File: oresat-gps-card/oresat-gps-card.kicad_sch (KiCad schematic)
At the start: 0 parts

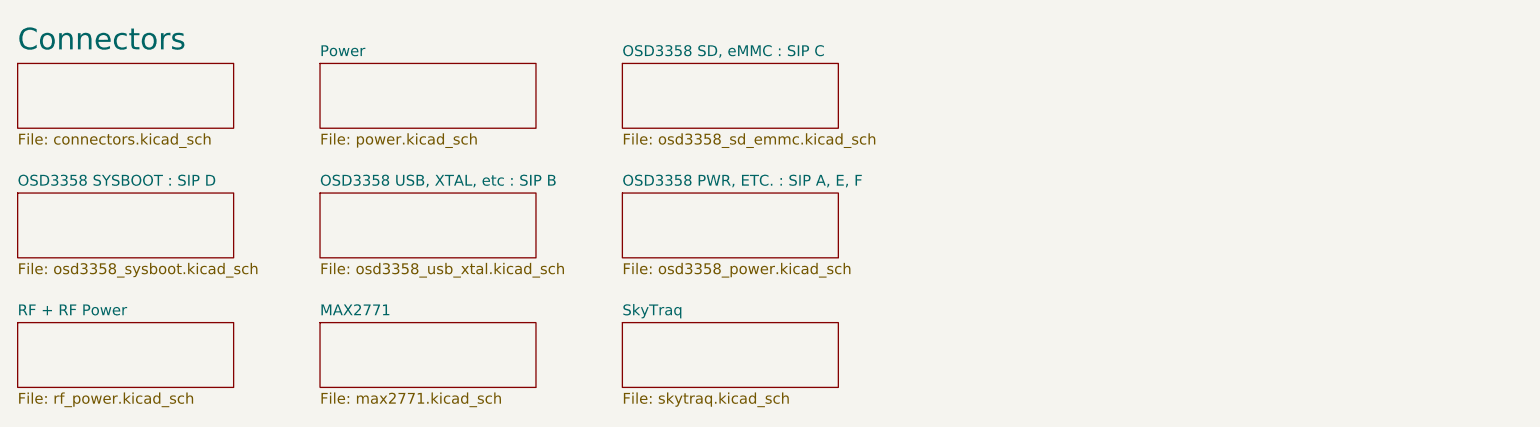
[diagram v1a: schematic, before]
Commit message: Updated schematic sheet links to match new naming
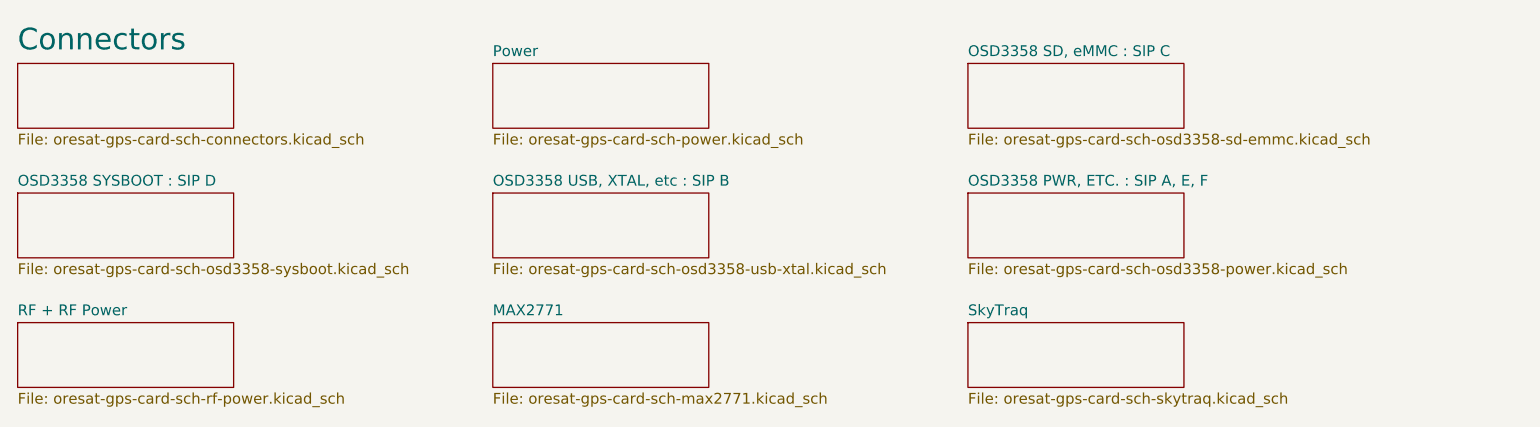
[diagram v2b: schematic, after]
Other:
- sheet Connectors: file connectors.kicad_sch -> oresat-gps-card-sch-connectors.kicad_sch
- sheet MAX2771: file max2771.kicad_sch -> oresat-gps-card-sch-max2771.kicad_sch
- sheet OSD3358 PWR, ETC. : SIP A, E, F: file osd3358_power.kicad_sch -> oresat-gps-card-sch-osd3358-power.kicad_sch
- sheet OSD3358 SD, eMMC : SIP C: file osd3358_sd_emmc.kicad_sch -> oresat-gps-card-sch-osd3358-sd-emmc.kicad_sch
- sheet OSD3358 SYSBOOT : SIP D: file osd3358_sysboot.kicad_sch -> oresat-gps-card-sch-osd3358-sysboot.kicad_sch
- sheet OSD3358 USB, XTAL, etc : SIP B: file osd3358_usb_xtal.kicad_sch -> oresat-gps-card-sch-osd3358-usb-xtal.kicad_sch
- sheet Power: file power.kicad_sch -> oresat-gps-card-sch-power.kicad_sch
- sheet RF + RF Power: file rf_power.kicad_sch -> oresat-gps-card-sch-rf-power.kicad_sch
- sheet SkyTraq: file skytraq.kicad_sch -> oresat-gps-card-sch-skytraq.kicad_sch

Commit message: Updated KiCAD 8, updated schematic sheet info, polished some schematic things, and made DNP parts DNP.
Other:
- title: (none) -> OreSat GPS Card

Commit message: Routine push
Began update to GPS chip
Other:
- removed sheet MAX2771
- added sheet MAX2769 (oresat-gps-card-sch-max2771.kicad_sch)
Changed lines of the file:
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@@
 (kicad_sch
-	(version 20250114)
+	(version 20260306)
 	(generator "eeschema")
-	(generator_version "9.0")
+	(generator_version "10.0")
 	(paper "B")
 	(title_block
@@
 		)
 		(fill
-			(color 0 0 0 0.0000)
+			(color 0 0 0 0)
 		)
 		(property "Sheetname" "OSD3358 PWR, ETC. : SIP A, E, F"
 			(at 185.42 80.5684 0)
+			(show_name no)
+			(do_not_autoplace no)
 			(effects
 				(font
@@
 		(property "Sheetfile" "oresat-gps-card-sch-osd3358-power.kicad_sch"
 			(at 185.42 89.4846 0)
+			(show_name no)
+			(do_not_autoplace no)
 			(effects
 				(font
@@
 		)
 		(fill
-			(color 0 0 0 0.0000)
+			(color 0 0 0 0)
 		)
 		(property "Sheetname" "OSD3358 SYSBOOT : SIP D"
 			(at 73.66 80.5684 0)
+			(show_name no)
+			(do_not_autoplace no)
 			(effects
 				(font
@@
 		(property "Sheetfile" "oresat-gps-card-sch-osd3358-sysboot.kicad_sch"
 			(at 73.66 89.4846 0)
+			(show_name no)
+			(do_not_autoplace no)
 			(effects
 				(font
@@
 		)
 		(fill
-			(color 0 0 0 0.0000)
+			(color 0 0 0 0)
 		)
 		(property "Sheetname" "OSD3358 USB, XTAL, etc : SIP B"
 			(at 129.54 80.5684 0)
+			(show_name no)
+			(do_not_autoplace no)
 			(effects
 				(font
@@
 		(property "Sheetfile" "oresat-gps-card-sch-osd3358-usb-xtal.kicad_sch"
 			(at 129.54 89.4846 0)
+			(show_name no)
+			(do_not_autoplace no)
 			(effects
 				(font
@@
 	)
 	(sheet
+		(at 129.54 66.04)
+		(size 25.4 7.62)
+		(exclude_from_sim no)
+		(in_bom yes)
+		(on_board yes)
+		(dnp no)
+		(fields_autoplaced yes)
+		(stroke
+			(width 0.1524)
+			(type solid)
+		)
+		(fill
+			(color 0 0 0 0)
+		)
+		(property "Sheetname" "Power"
+			(at 129.54 65.3284 0)
+			(show_name no)
+			(do_not_autoplace no)
+			(effects
+				(font
+					(size 1.27 1.27)
+				)
+				(justify left bottom)
+			)
+		)
+		(property "Sheetfile" "oresat-gps-card-sch-power.kicad_sch"
+			(at 129.54 74.2446 0)
+			(show_name no)
+			(do_not_autoplace no)
+			(effects
+				(font
+					(size 1.27 1.27)
+				)
+				(justify left top)
+			)
+		)
+		(instances
+			(project "oresat-gps-card"
+				(path "/65d12cdd-c326-4033-9053-c59fa4e0b25e"
+					(page "2")
+				)
+			)
+		)
+	)
+	(sheet
 		(at 129.54 96.52)
 		(size 25.4 7.62)
@@
 		)
 		(fill
-			(color 0 0 0 0.0000)
-		)
-		(property "Sheetname" "MAX2771"
+			(color 0 0 0 0)
+		)
+		(property "Sheetname" "MAX2769"
 			(at 129.54 95.8084 0)
+			(show_name no)
+			(do_not_autoplace no)
 			(effects
 				(font
@@
 		(property "Sheetfile" "oresat-gps-card-sch-max2771.kicad_sch"
 			(at 129.54 104.7246 0)
-			(effects
-				(font
-					(size 1.27 1.27)
-				)
-				(justify left top)
-			)
-		)
-		(instances
-			(project "oresat-gps-card"
-				(path "/65d12cdd-c326-4033-9053-c59fa4e0b25e"
-					(page "8")
-				)
-			)
-		)
-	)
-	(sheet
-		(at 129.54 66.04)
-		(size 25.4 7.62)
-		(exclude_from_sim no)
-		(in_bom yes)
-		(on_board yes)
-		(dnp no)
-		(fields_autoplaced yes)
-		(stroke
-			(width 0.1524)
-			(type solid)
-		)
-		(fill
-			(color 0 0 0 0.0000)
-		)
-		(property "Sheetname" "Power"
-			(at 129.54 65.3284 0)
-			(effects
-				(font
-					(size 1.27 1.27)
-				)
-				(justify left bottom)
-			)
-		)
-		(property "Sheetfile" "oresat-gps-card-sch-power.kicad_sch"
-			(at 129.54 74.2446 0)
-			(effects
-				(font
-					(size 1.27 1.27)
-				)
-				(justify left top)
-			)
-		)
-		(instances
-			(project "oresat-gps-card"
-				(path "/65d12cdd-c326-4033-9053-c59fa4e0b25e"
-					(page "2")
+			(show_name no)
+			(do_not_autoplace no)
+			(effects
+				(font
+					(size 1.27 1.27)
+				)
+				(justify left top)
+			)
+		)
+		(instances
+			(project "oresat-gps-card"
+				(path "/65d12cdd-c326-4033-9053-c59fa4e0b25e"
+					(page "10")
 				)
 			)
@@
 		)
 		(fill
-			(color 0 0 0 0.0000)
+			(color 0 0 0 0)
 		)
 		(property "Sheetname" "RF + RF Power"
 			(at 73.66 95.8084 0)
+			(show_name no)
+			(do_not_autoplace no)
 			(effects
 				(font
@@
 		(property "Sheetfile" "oresat-gps-card-sch-rf-power.kicad_sch"
 			(at 73.66 104.7246 0)
+			(show_name no)
+			(do_not_autoplace no)
 			(effects
 				(font
@@
 		)
 		(fill
-			(color 0 0 0 0.0000)
+			(color 0 0 0 0)
 		)
 		(property "Sheetname" "Connectors"
 			(at 73.66 64.6934 0)
+			(show_name no)
+			(do_not_autoplace no)
 			(effects
 				(font
@@
 		(property "Sheetfile" "oresat-gps-card-sch-connectors.kicad_sch"
 			(at 73.66 74.2446 0)
+			(show_name no)
+			(do_not_autoplace no)
 			(effects
 				(font
@@
 		)
 		(fill
-			(color 0 0 0 0.0000)
+			(color 0 0 0 0)
 		)
 		(property "Sheetname" "OSD3358 SD, eMMC : SIP C"
 			(at 185.42 65.3284 0)
+			(show_name no)
+			(do_not_autoplace no)
 			(effects
 				(font
@@
 		(property "Sheetfile" "oresat-gps-card-sch-osd3358-sd-emmc.kicad_sch"
 			(at 185.42 74.2446 0)
+			(show_name no)
+			(do_not_autoplace no)
 			(effects
 				(font
@@
 		)
 		(fill
-			(color 0 0 0 0.0000)
+			(color 0 0 0 0)
 		)
 		(property "Sheetname" "SkyTraq"
 			(at 185.42 95.8084 0)
+			(show_name no)
+			(do_not_autoplace no)
 			(effects
 				(font
@@
 		(property "Sheetfile" "oresat-gps-card-sch-skytraq.kicad_sch"
 			(at 185.42 104.7246 0)
-			(effects
-				(font
+			(show_name no)
+			(do_not_autoplace no)
+			(effects
+				(font

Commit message: Routine Push
First attempt to clean up schematic
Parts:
- added CM1: J-MOLEX-SMPM-73300-003X, oresat-connectors:J-MOLEX-SMPM-073300-002X, symbol oresat-connectors:J-MOLEX-SMPM-73300-002X
- added FID1, FID2, FID3, FID4, FID5, FID6: Fiducial, Fiducial:Fiducial_1mm_Mask2mm, symbol Mechanical:Fiducial
- added FLIGHT1: FLIGHTMARKER, oresat-graphics:FLIGHTMARKER, symbol oresat-graphics:FLIGHTMARKER
- added J1: J-SAMTEC-TFM-120-01-L-D-RA, oresat-connectors:J-SAMTEC-TFM-120-X1-XXX-D-RA, symbol oresat-connectors:J-SAMTEC-TFM-120-01-L-D-RA
- added J3: GRPB041VWVN-RC, Connector_PinHeader_1.27mm:PinHeader_1x04_P1.27mm_Vertical, symbol Connector_Generic:Conn_01x04
- added J6: SM14B-SHLS-TF, oresat-connectors:J-JST-SM14BSHLSTF, symbol oresat-connectors:ORESAT-DEBUG-CONNECTOR-3
- added PCB1: ORESAT-CARD-V1.3-GENERIC-1RF-POS2, oresat-pcbs:ORESAT-CARD-V1.3-1RF-POS2, symbol oresat-pcbs:ORESAT-CARD-V1.3-1RF-POS2
- added R68: 75, Resistor_SMD:R_0603_1608Metric, symbol Device:R_US
- added TP140, TP141, TP159: 0.03x0.04, oresat-misc:TestPoint_Pad_D1.0mm, symbol oresat-misc:Test-Point-1mm-round
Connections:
- new net: J6.10 (NRST), R68.1
- new net: J6.8 (DEBUG-0), TP159.1
- new net C3-UART-RX: J1.38
- new net C3-UART-TX: J1.37
- new net CAN1_H: J1.33, J1.34, TP140.1
- new net CAN1_L: J1.35, J1.36, TP141.1
- new net CAN2_H: J1.17, J1.18
- new net CAN2_L: J1.19, J1.20
- new net EEPROM_WP: J3.2 (Pin_2)
- new net GND: CM1.SHLD, J1.27, J1.28, J1.29, J1.30, J3.1 (Pin_1), J6.14 (GND), J6.15 (PAD), J6.16 (PAD), J6.5 (GND)
- new net OPD_PWR: J1.15, J1.16
- new net OPD_SCL: J1.13, J1.14
- new net OPD_SDA: J1.11, J1.12
- new net PMIC_SCL: J3.4 (Pin_4)
- new net PMIC_SDA: J3.3 (Pin_3)
- new net RF-IN: CM1.SIG
- new net UART0_RX: J6.7 (CARD-RX)
- new net UART0_TX: J6.6 (CARD-TX)
- new net USB_CLI_N: J6.4 (DEVICE-D-)
- new net USB_CLI_P: J6.3 (DEVICE-D+)
- new net USB_CLI_VBUS: J6.1 (VBUSP), J6.2 (VBUSP)
- new net VBUS: J1.23, J1.24, J1.25, J1.26
- new net nRESET: R68.2
- new net ~{SD}: J1.39, J1.40
- no-connect marks 0 -> 18
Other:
- removed sheet Connectors
- sheet MAX2769 ports: added I0, I1, MAX-CLKOUT, MAX-RF, MAX_SPI1_CS0, MAX_SPI1_D0, MAX_SPI1_SCLK, MAX_~{SHDN}, Q0, Q1; removed none
- sheet OSD3358 PWR, ETC. : SIP A, E, F ports: added EEPROM_WP, I2C0_SCL, I2C0_SDA, PMIC_SCL, PMIC_SDA, VIN_USB, nRESET; removed none
- sheet OSD3358 SD, eMMC : SIP C ports: added CAN2_H, CAN2_L, I0, I1, MAX-CLKOUT, Q0, Q1, UART0_RX, UART0_TX; removed none
- sheet OSD3358 SYSBOOT : SIP D ports: added GPS-EN, MAX-LD, MAX_SPI1_CS0, MAX_SPI1_D0, MAX_SPI1_SCLK, MAX_~{SHDN}, STQ-1PPS, STQ_UART2_RX, STQ_UART2_TX, SYSBOOT2; removed none
- sheet OSD3358 USB, XTAL, etc : SIP B ports: added USB_CLI_N, USB_CLI_P, USB_CLI_VBUS, VIN_USB, nRESET; removed none
- sheet Power ports: added C3-UART-RX, C3-UART-TX, OPD_PWR, OPD_SCL, OPD_SDA, SYSBOOT2, UART0_RX, UART0_TX; removed none
- sheet RF + RF Power ports: added GPS-EN, MAX-RF, RF-IN, STQ-RF; removed none
- sheet SkyTraq ports: added STQ-1PPS, STQ-RF, STQ_UART2_RX, STQ_UART2_TX; removed none
- note added: "Fiducials (on both sides of board)"
- note added: "Main Backplane Connector"
- note added: "Main OreSat Card Connector"
- note added: "Oresat Debug Connector"
- note added: "RF SMPM Connector"
